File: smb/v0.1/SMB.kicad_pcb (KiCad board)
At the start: 2 copper layers, 88 parts, among them IC101 ATMEGA1284-A, J101 RJ45, J102 RTS_RESET, J103 ICSP, J104 SERIAL_REV, J202 USD_CONN, J401 HR911105_RJ45, P1 CONN_2, P101 I2C_CONN, P102 CONN_3X2, P103 CONN_3X2, P104 CONN_3X2, P105 CONN_5, P106 CONN_3X2, P107 CONN_7, P108 CONN_5, P301 CONN_2, SW101 SKQGAKE010, U201 ENC28J60, U202 LM1117IMP-3.3, U203 74LVC1G126GW, U204 74LVC1G126GW, U205 74LVC1G126GW, U206 74LVC1G126GW, U301 74HC08, U302 MP2562DS, X101 20MHz, X201 25MHz

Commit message: Update draft PCB SmBV0.1
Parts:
- moved P105 212.0 mm to (243.9, 30.2)
- moved P108 121.4 mm to (167.8, 33.8)
- moved R102 77.6 mm to (87.6, 108.0), turned to 0 degrees
- moved D101 77.3 mm to (79.2, 107.4)
- moved P104 76.2 mm to (180.0, 46.8), turned to 0 degrees
- moved U203 63.7 mm to (66.8, 45.0)
- moved J103 57.3 mm to (75.2, 56.8)
- moved U204 57.2 mm to (70.0, 45.0)
- moved C215 56.1 mm to (60.2, 43.8)
- moved J202 52.9 mm to (70.6, 35.0), turned to 180 degrees
- moved U205 50.8 mm to (73.2, 45.0)
- moved U206 44.3 mm to (76.4, 45.0)
- moved R103 41.0 mm to (79.6, 45.4), turned to 90 degrees
- moved R104 36.4 mm to (71.6, 94.0), turned to 270 degrees
- moved R401 34.4 mm to (35.6, 60.0), turned to 90 degrees
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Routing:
- net GND: track 708.4 -> 111.6 mm, vias 10 -> 12
- net +5V: track 555.6 -> 234.2 mm, vias 16 -> 6
- net SCL: track 199.7 -> 69.6 mm, vias 7 -> 1
- net SDA: track 187.5 -> 57.9 mm, vias 6 -> 2
- net /INT_I2C: track 130.6 -> 28.4 mm, vias 1 -> 0
- net SPI_MOSI: track 143.7 -> 57.5 mm, vias 7 -> 3
- net SPI_CLK: track 155.9 -> 73.6 mm, vias 7 -> 3
- net RX1: track 76.1 -> 0.00 mm, vias 3 -> 0
- net TX1: track 71.5 -> 0.00 mm, vias 1 -> 0
- net PD4: track 67.1 -> 0.00 mm, vias 1 -> 0
- net PC3: track 64.4 -> 0.00 mm, vias 1 -> 0
- net DS: track 59.9 -> 0.00 mm, vias 2 -> 0
- net PC2: track 57.3 -> 0.00 mm, vias 1 -> 0
- net PC5: track 57.0 -> 0.00 mm
- net PC4: track 53.8 -> 0.00 mm, vias 1 -> 0
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- added copper zone on F.Cu, net +3.3V
- added copper zone on F.Cu, net +5V
- added copper zone on F.Cu, net GND
- added copper zone on F.Cu, net N-0000063
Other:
- net class 12V added: clearance 0.254, trace_width 0.508, via_dia 0.889, via_drill 0.635
- net class Default: trace_width 0.2032 -> 0.3

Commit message: Update PCB SMB V0.1
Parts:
- moved P105 118.3 mm to (130.5, 63.8), turned to 270 degrees
- moved P104 75.2 mm to (108.0, 68.5), turned to 270 degrees
- moved P108 55.2 mm to (121.5, 63.8), turned to 270 degrees
- moved D102 28.6 mm to (61.0, 109.8)
- moved R1 28.6 mm to (57.8, 109.8)
- moved P107 25.6 mm to (106.0, 85.0), turned to 180 degrees
- moved P106 21.6 mm to (105.8, 53.8), turned to 0 degrees
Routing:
- net GND: track 111.6 -> 241.6 mm, vias 12 -> 22
- net +5V: track 234.2 -> 351.5 mm, vias 6 -> 7
- net PC2: track 0.00 -> 63.8 mm, vias 0 -> 1
- net PC4: track 0.00 -> 63.7 mm, vias 0 -> 1
- net DS: track 0.00 -> 62.4 mm, vias 0 -> 2
- net /INT_I2C: track 28.4 -> 86.7 mm, vias 0 -> 2
- net PC5: track 0.00 -> 58.0 mm, vias 0 -> 2
- net PC3: track 0.00 -> 53.6 mm, vias 0 -> 1
- net TX1: track 0.00 -> 50.8 mm
- net N-000004: track 0.00 -> 50.7 mm, vias 0 -> 2
- net RX1: track 0.00 -> 49.8 mm
- net PC6: track 0.00 -> 48.9 mm, vias 0 -> 1
- net SDA: track 57.9 -> 99.9 mm
- net PD4: track 0.00 -> 40.4 mm, vias 0 -> 1
- net SCL: track 69.6 -> 109.8 mm, vias 1 -> 2
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- added copper zone on B.Cu, net GND
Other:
- board text removed: "C203 -> Pin 28 C204 -> Pin 15 C205 -> Pin 19 C206 -> Pin 25 C207 -> Pin 20 C208 -> Pin 01 R201 -> Pin 14 Au plus proche"

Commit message: routage complet ajout rs485 attention, tous les packages sont ? v?rifier
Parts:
- added GS2: GS2, GS2, F.Cu at (119.3, 40.3)
- added GS3: GS2, GS2, F.Cu at (115.3, 40.3)
- added IC1: SP3485CN, SO8E, F.Cu at (95.0, 43.8)
- added R2: R, SM1206, F.Cu at (101.0, 39.4)
- added R3: R, SM1206, F.Cu at (121.5, 43.3)
- added R4: R, SM1206, F.Cu at (114.3, 43.3)
- D102: footprint LED-0603 -> LED-1206
- P107: value CONN_7 -> CONN_3; footprint HE10-6 -> MOL_CONN_5_MINI
- R1: footprint SM0603 -> SM1206
- moved P107 54.0 mm to (122.4, 33.5)
- moved D101 28.2 mm to (107.3, 105.9), turned to 180 degrees
- moved P106 22.2 mm to (107.2, 75.9), turned to 270 degrees
- moved SW101 21.1 mm to (92.7, 107.7)
- moved R103 18.9 mm to (89.9, 61.2), turned to 180 degrees
- moved J102 15.6 mm to (91.3, 102.1), turned to 0 degrees
- moved P104 14.8 mm to (105.7, 53.8), turned to 0 degrees
- moved R102 13.9 mm to (101.3, 105.9), turned to 180 degrees
- moved R204 11.5 mm to (47.2, 47.6), turned to 0 degrees
- moved R203 9.35 mm to (47.2, 50.2)
- moved C215 9.17 mm to (69.3, 44.5), turned to 180 degrees
- moved C310 7.12 mm to (39.8, 96.6), turned to 180 degrees
- moved R201 6.52 mm to (64.2, 51.6), turned to 0 degrees
- moved P102 6.47 mm to (86.9, 90.4)
- moved P1 5.91 mm to (40.0, 91.3)
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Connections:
- net N-0000063 renamed pre_5V
- IC101 pad 13: PD4 -> LED_STATUS
- IC101 pad 14: PD5 -> N-000004
- IC101 pad 15: LED_STATUS -> PD6
- IC101 pad 24: PC5 -> DS
- IC101 pad 40: DS -> PB0
- IC101 pad 41: N-000004 -> (no net)
- P102 pad 2: RX0 -> LED_STATUS
- P102 pad 5: LED_STATUS -> RX0
- P106 pad 2: PC2 -> PC4
- P106 pad 3: PC3 -> PC2
- P106 pad 4: PC4 -> PC3
- P106 pad 5: PC5 -> PD6
- P107 pad 1: +5V -> GND
- P107 pad 2: GND -> TX+
- P107 pad 3: TX1 -> TX-
- P107 pad 4: RX1 -> TX+
- P107 pad 5: PD5 -> N-0000024
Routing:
- net GND: track 241.6 -> 114.2 mm, vias 22 -> 11
- net PC5: track 58.0 -> 0.00 mm, vias 2 -> 0
- net /RESET: track 175.0 -> 118.4 mm, vias 6 -> 2
- net PC4: track 63.7 -> 14.3 mm
- net PC2: track 63.8 -> 15.3 mm
- net TX+: track 0.00 -> 46.6 mm
- net PD4: track 40.4 -> 0.00 mm, vias 1 -> 0
- net PD5: track 39.3 -> 0.00 mm, vias 1 -> 0
- net PC3: track 53.6 -> 15.7 mm
- net PB0: track 0.00 -> 37.5 mm, vias 0 -> 2
- net +5V: track 351.5 -> 386.6 mm, vias 7 -> 5
- net +3.3V: track 156.7 -> 128.1 mm, vias 5 -> 4
- net RX0: track 75.6 -> 47.0 mm
- net SPI_CLK: track 73.6 -> 45.6 mm, vias 3 -> 2
- net TX-: track 0.00 -> 26.5 mm
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
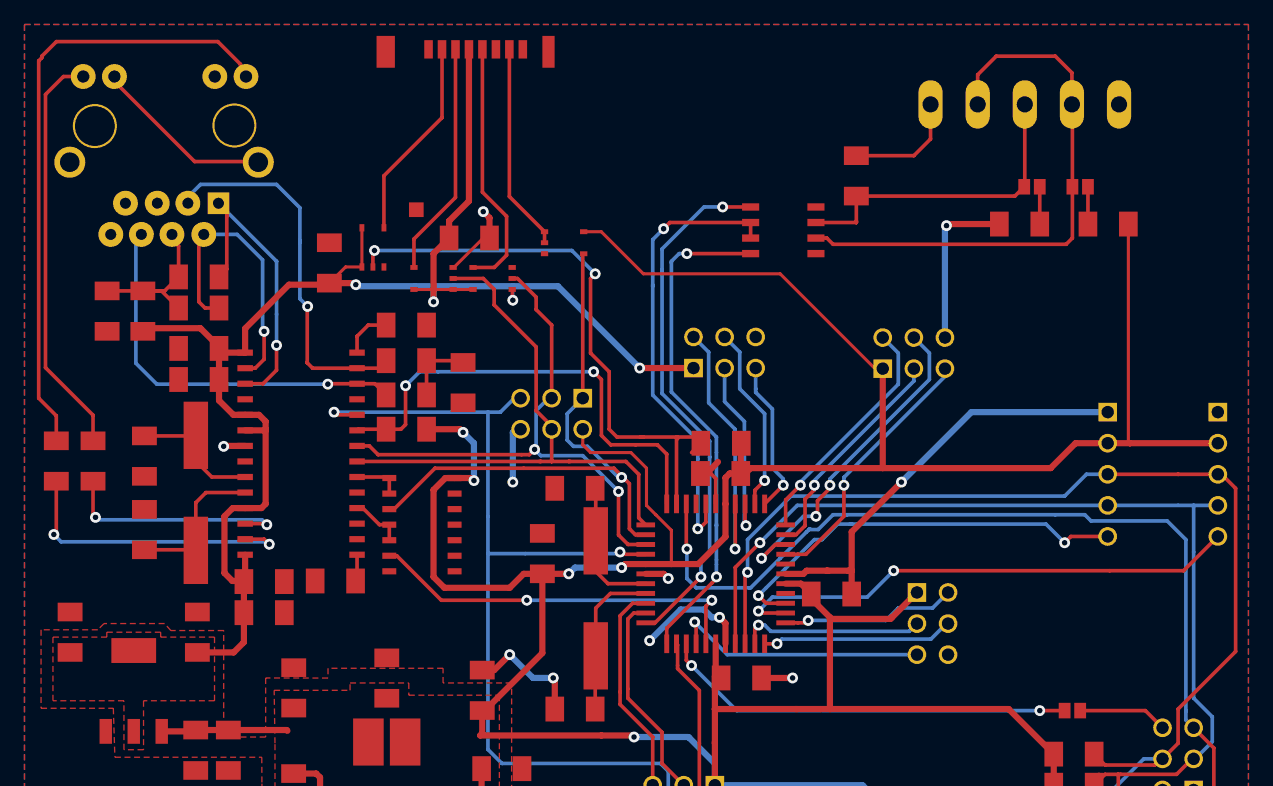
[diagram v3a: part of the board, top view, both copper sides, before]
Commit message: routage, reprise plan de masse, suppression de vias
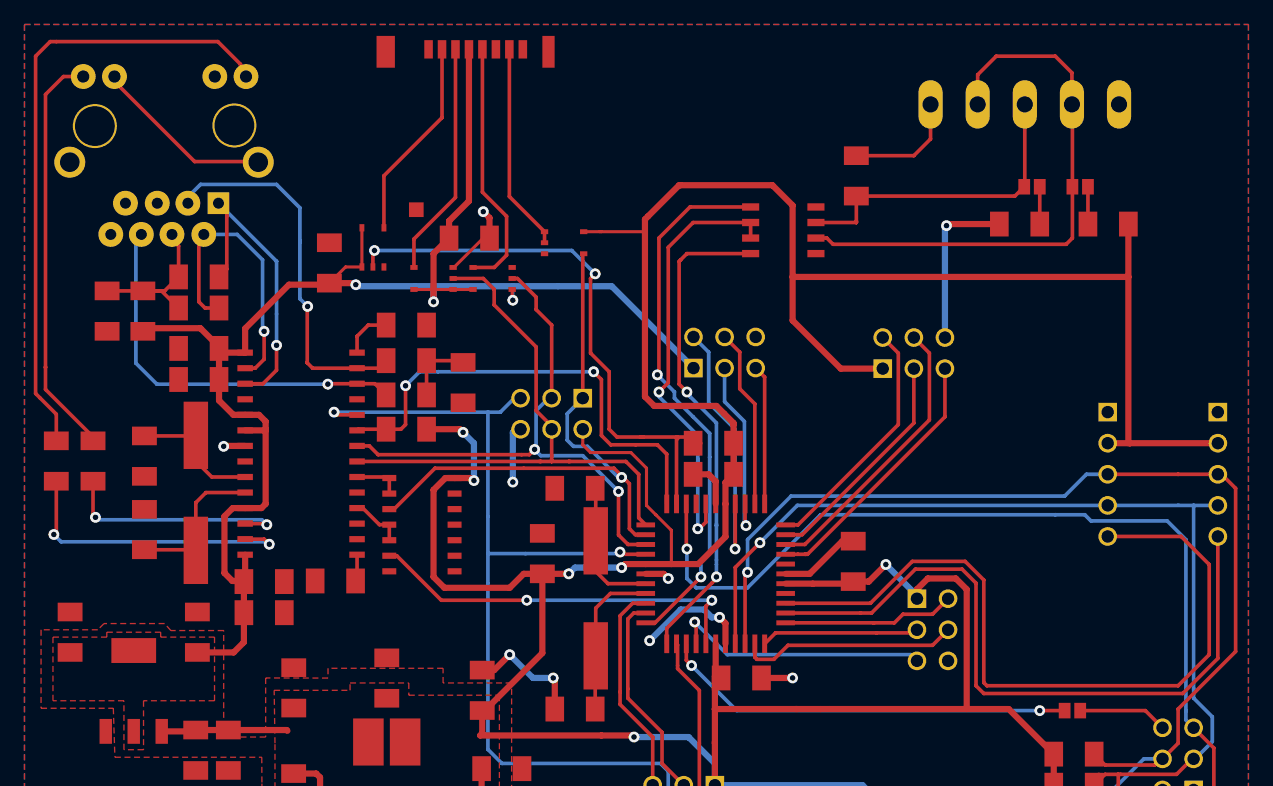
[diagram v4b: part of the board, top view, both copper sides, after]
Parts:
- moved C102 3.21 mm to (100.7, 70.9), turned to 90 degrees
- moved R103 0.63 mm to (89.3, 61.2)
- moved C103 0.60 mm to (89.3, 63.8)
- moved P106 0.51 mm to (107.2, 76.5)
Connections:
- P106 pad 3: PC2 -> PC3
- P106 pad 4: PC3 -> PC2
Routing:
- net GND: track 114.2 -> 82.5 mm, vias 11 -> 10
- net PC6: track 34.4 -> 62.8 mm, vias 2 -> 0
- net +5V: track 386.6 -> 412.8 mm, vias 5 -> 6
- net DS: track 42.4 -> 57.1 mm, vias 2 -> 0
- net PA6: track 27.3 -> 23.2 mm, vias 3 -> 0
- net PC3: track 15.7 -> 12.9 mm, vias 1 -> 0
- net PC2: track 15.3 -> 18.0 mm, vias 1 -> 0
- net PB0: track 37.5 -> 36.1 mm
- net PA3: track 12.7 -> 11.4 mm, vias 1 -> 0
- net uSD_CS: track 48.5 -> 47.6 mm
- net TX1: track 41.3 -> 40.4 mm
- net RX1: track 43.7 -> 44.5 mm
- net PA2: track 15.3 -> 14.7 mm, vias 1 -> 0
- net PA4: track 19.6 -> 20.2 mm, vias 1 -> 0
- net N-0000059: track 50.6 -> 51.1 mm
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
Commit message: M?J Piste, Plan de masse, Via
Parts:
- moved P102 3.47 mm to (90.2, 91.4)
- moved R201 0.60 mm to (63.6, 51.6)
- moved C214 0.45 mm to (47.1, 77.1)
- moved C213 0.35 mm to (36.7, 77.0)
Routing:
- net GND: track 82.5 -> 50.3 mm, vias 10 -> 7
- net N-0000055: track 32.1 -> 63.9 mm, vias 1 -> 0
- net PA1: track 15.4 -> 30.0 mm, vias 1 -> 0
- net TX+: track 46.6 -> 60.2 mm
- net /RESET: track 118.4 -> 128.1 mm
- net PC6: track 62.8 -> 71.9 mm
- net N-000004: track 34.0 -> 41.5 mm, vias 2 -> 0
- net N-0000056: track 19.1 -> 26.3 mm, vias 2 -> 0
- net N-0000057: track 23.2 -> 16.1 mm, vias 1 -> 0
- net RX0: track 47.0 -> 52.9 mm
- net SDA: track 94.5 -> 99.4 mm
- net PA7: track 21.7 -> 26.2 mm
- net PD6: track 21.3 -> 25.9 mm, vias 1 -> 0
- net PA6: track 23.2 -> 27.6 mm
- net PA5: track 18.7 -> 22.8 mm
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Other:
- board outline added: 100 x 86 mm

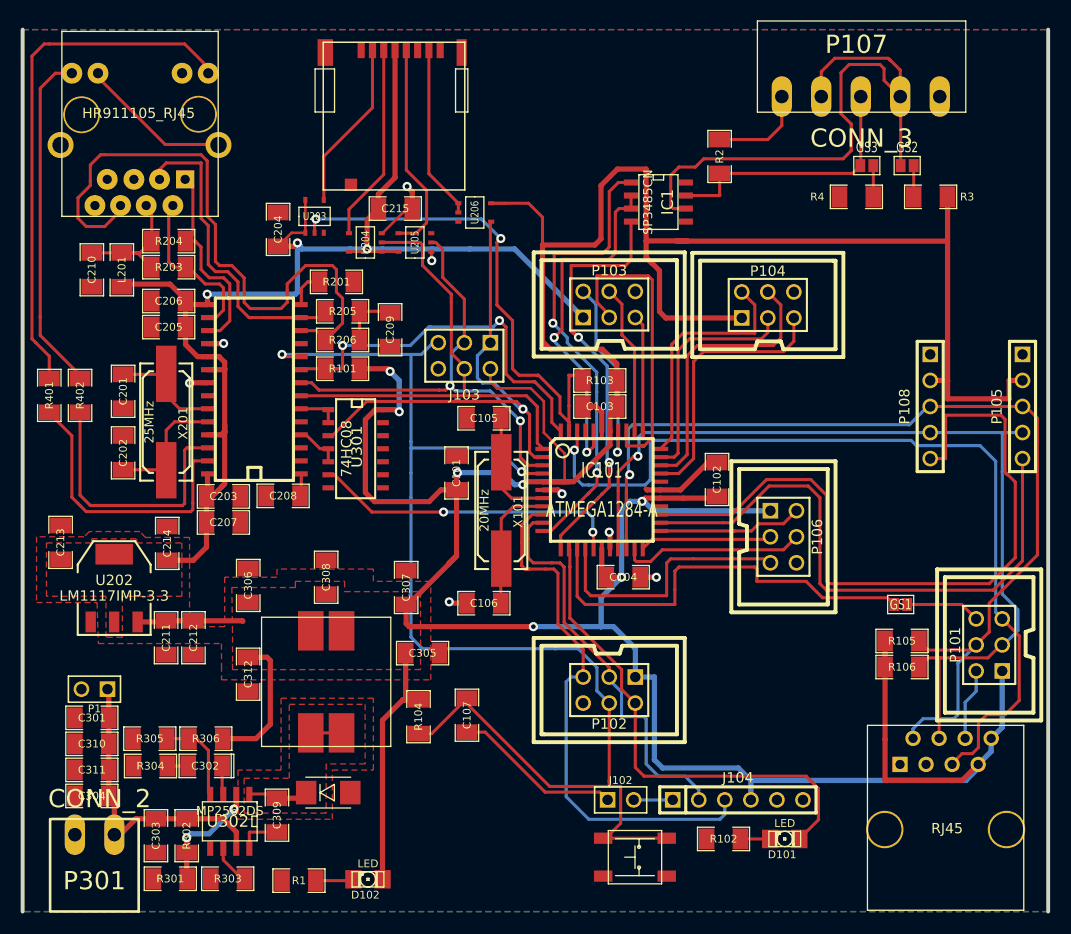
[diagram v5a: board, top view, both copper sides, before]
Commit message: correction broche 8 du module RS485 + inversion tx+/tx- au niveau du connecteur + pilotage E/R independant inversion polarit? connecteur d'alim d?placement slot pour rtc simplification routage et optimisation plan de masse (affinage zone exclusion)
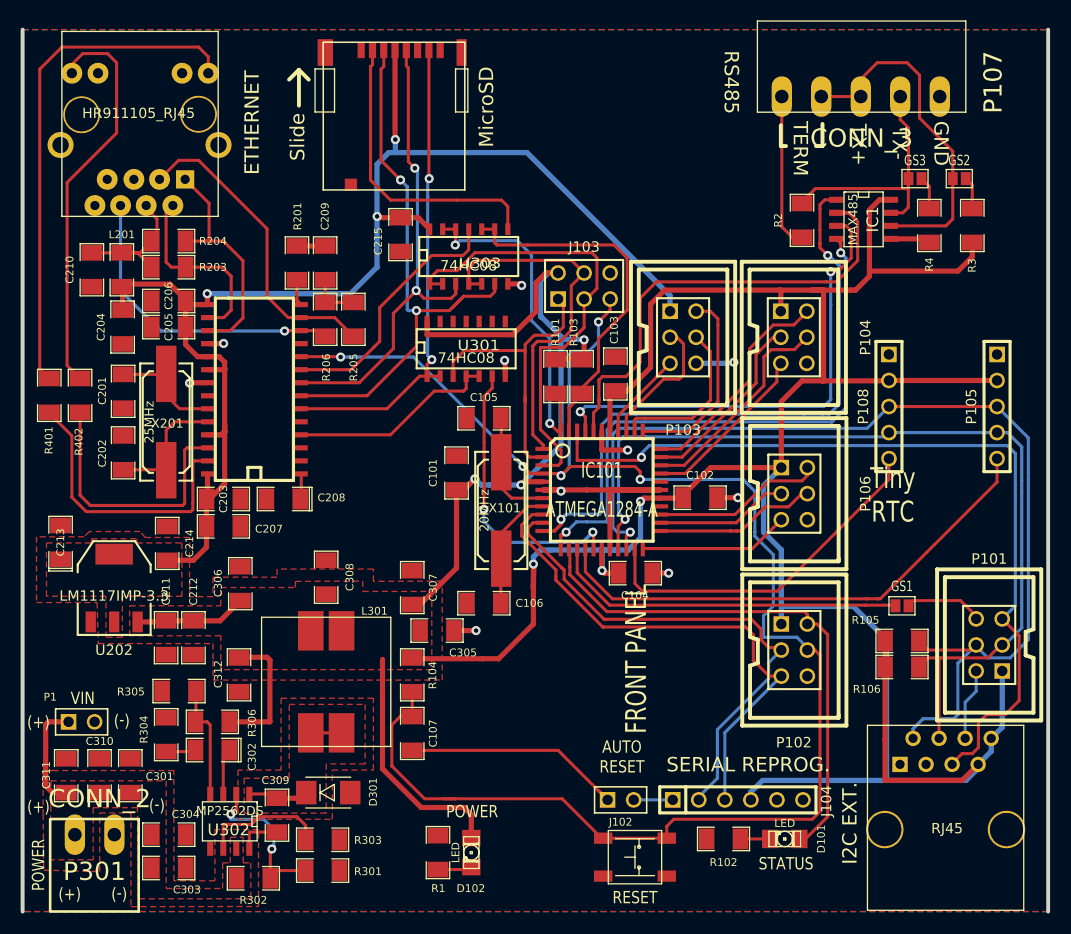
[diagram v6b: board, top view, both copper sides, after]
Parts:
- removed U203, U204, U205, U206: 74LVC1G126GW, SOT753
- added U303: 74HC08, SO14E, F.Cu at (76.5, 49.0)
- C208, C213: footprint SM1206 -> SM1206POL
- IC1: value SP3485CN -> MAX485
- R201: value 2k7 -> 2k32
- moved R101 20.8 mm to (85.0, 60.8), turned to 270 degrees
- moved IC1 20.1 mm to (115.0, 45.5)
- moved P102 18.5 mm to (108.2, 87.5), turned to 270 degrees
- moved C204 17.9 mm to (42.8, 56.0), turned to 90 degrees
- moved R301 14.9 mm to (62.2, 109.0), turned to 0 degrees
- moved U301 14.5 mm to (76.2, 58.0), turned to 0 degrees
- moved R1 13.8 mm to (73.5, 107.2), turned to 90 degrees
- moved J103 13.5 mm to (87.8, 52.0), turned to 0 degrees
- moved D102 10.4 mm to (76.8, 107.2), turned to 270 degrees
- moved R2 10.2 mm to (109.0, 45.6), turned to 270 degrees
- moved R303 10.0 mm to (62.2, 106.0), turned to 0 degrees
- moved C209 9.08 mm to (62.5, 49.8), turned to 90 degrees
- moved C304 8.39 mm to (47.2, 105.5), turned to 0 degrees
- moved P103 7.88 mm to (97.4, 57.0), turned to 270 degrees
- moved R302 7.71 mm to (55.5, 109.8), turned to 0 degrees
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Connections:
- net +3.3V renamed 3.3V
- IC1 pad 3: PB0 -> PB1
- IC1 pad 8: (no net) -> +5V
- IC101 pad 15: PD6 -> DS
- IC101 pad 24: DS -> PC5
- IC101 pad 26: (no net) -> N-0000026
- IC101 pad 29: (no net) -> N-0000027
- IC101 pad 41: (no net) -> PB1
- J202 pad 1: (no net) -> N-0000082
- J202 pad 8: (no net) -> N-0000083
- J401 pad 5: (no net) -> N-0000054
- P103 pad 2: PA0 -> PA3
- P103 pad 5: PA3 -> PA0
- P106 pad 2: PC4 -> PC6
- P106 pad 3: PC3 -> PC5
- P106 pad 4: PC2 -> PC4
- P106 pad 5: PD6 -> PC3
- P107 pad 2: TX+ -> TX-
- P107 pad 3: TX- -> TX+
- P108 pad 5: PC6 -> PC2
- P301 pad 1: GND -> +12V
- P301 pad 2: +12V -> GND
- U201 pad 3: (no net) -> N-0000067
- U201 pad 6: N-0000051 (its old number) -> MISO_33
- U201 pad 7: SPI_MOSI -> MOSI_33
- U201 pad 8: SPI_CLK -> CLK_33
- U201 pad 9: ETH_CS -> ETH_CS_33
- U301 pad 1: N-0000051 (its old number) -> MISO_33
- U301 pad 2: N-0000051 (its old number) -> MISO_33
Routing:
- net PC6: track 71.9 -> 16.7 mm
- net PB1: track 0.00 -> 46.4 mm, vias 0 -> 2
- net /RESET: track 128.1 -> 166.6 mm, vias 2 -> 5
- net MOSI_33: track 19.2 -> 55.4 mm, vias 0 -> 2
- net +5V: track 413.0 -> 378.5 mm, vias 7 -> 6
- net N-0000050: track 63.9 -> 30.3 mm, vias 0 -> 1
- net MISO_33: track 17.0 -> 47.3 mm, vias 0 -> 2
- net CLK_33: track 20.8 -> 48.3 mm, vias 0 -> 2
- net TX+: track 60.2 -> 34.1 mm
- net PD6: track 25.9 -> 0.00 mm
- net ETH_CS_33: track 0.00 -> 25.1 mm
- net SPI_MISO: track 48.7 -> 29.2 mm, vias 1 -> 0
- net +12V: track 29.2 -> 10.6 mm
- net PC2: track 18.0 -> 35.0 mm
- net RX1: track 46.0 -> 63.1 mm
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- added copper zone on F.Cu, net +12V
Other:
- board text added: "(+)"
- board text added: "(-)"
- board text added: "AUTO RESET"
- board text added: "ETHERNET"
- board text added: "FRONT PANEL"
- board text added: "GND"
- board text added: "I2C EXT."
- board text added: "MicroSD"
- board text added: "POWER"
- board text added: "RESET"
- board text added: "RS485"
- board text added: "SERIAL REPROG."
- board text added: "STATUS"
- board text added: "Slide"
- board text added: "TERM"
- board text added: "TX+"
- board text added: "TX-"
- board text added: "VIN"
